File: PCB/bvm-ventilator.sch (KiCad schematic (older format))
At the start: 6 parts, among them U1 IEC_CONNECTOR

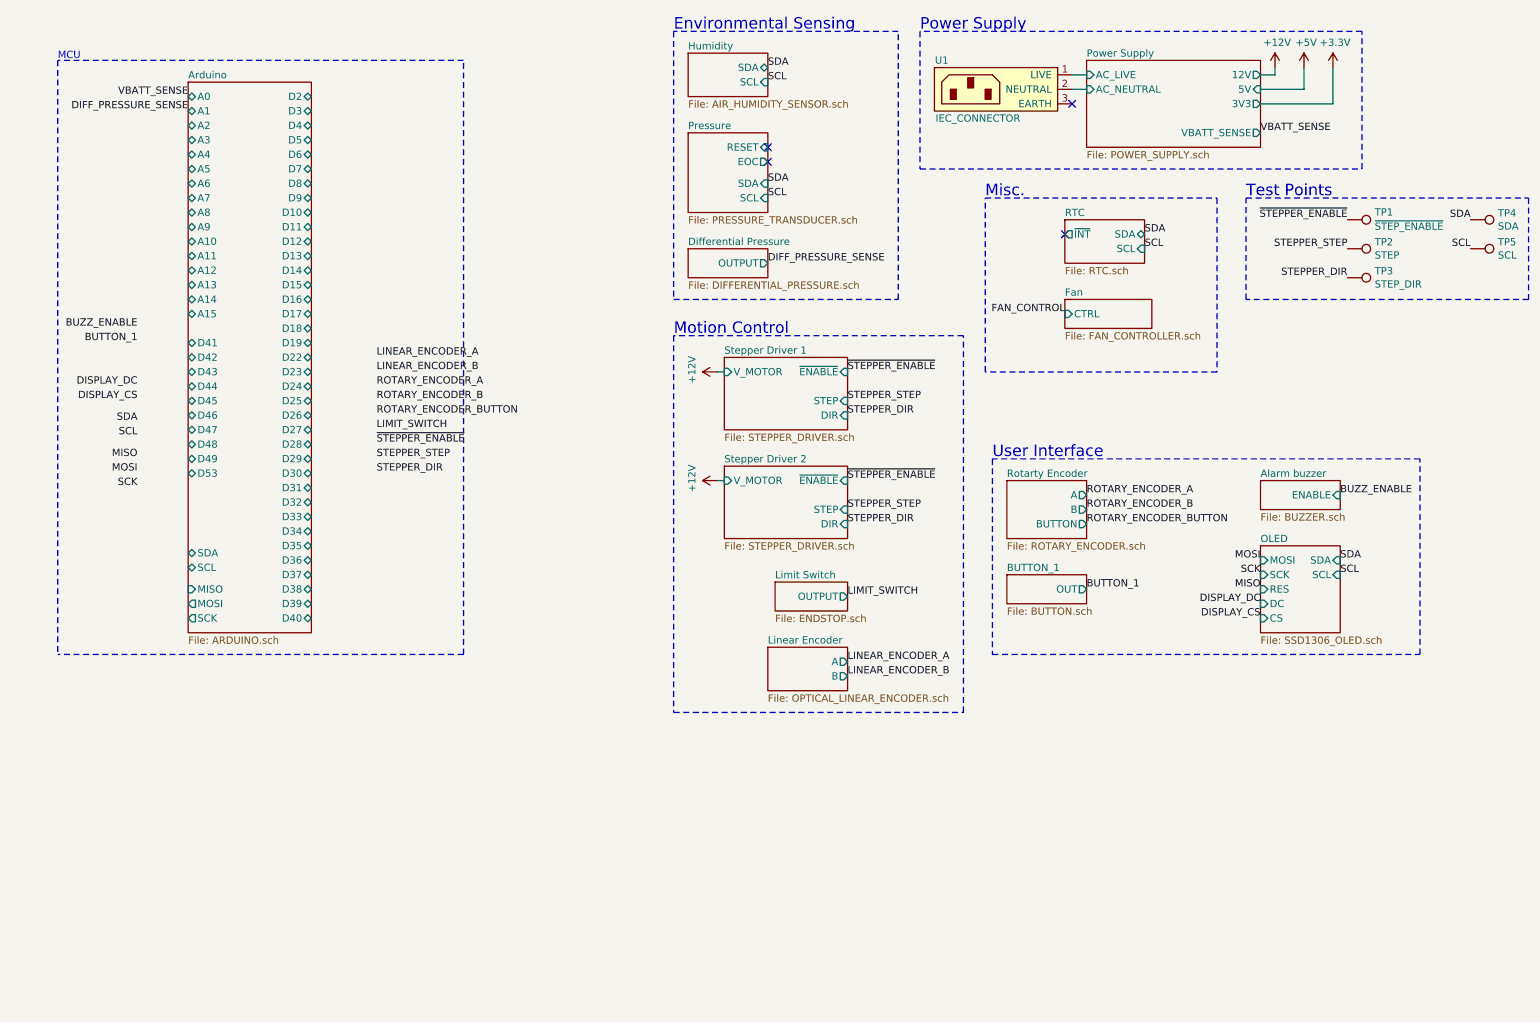
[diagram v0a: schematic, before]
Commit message: Connected all unconnected control/indicator pins
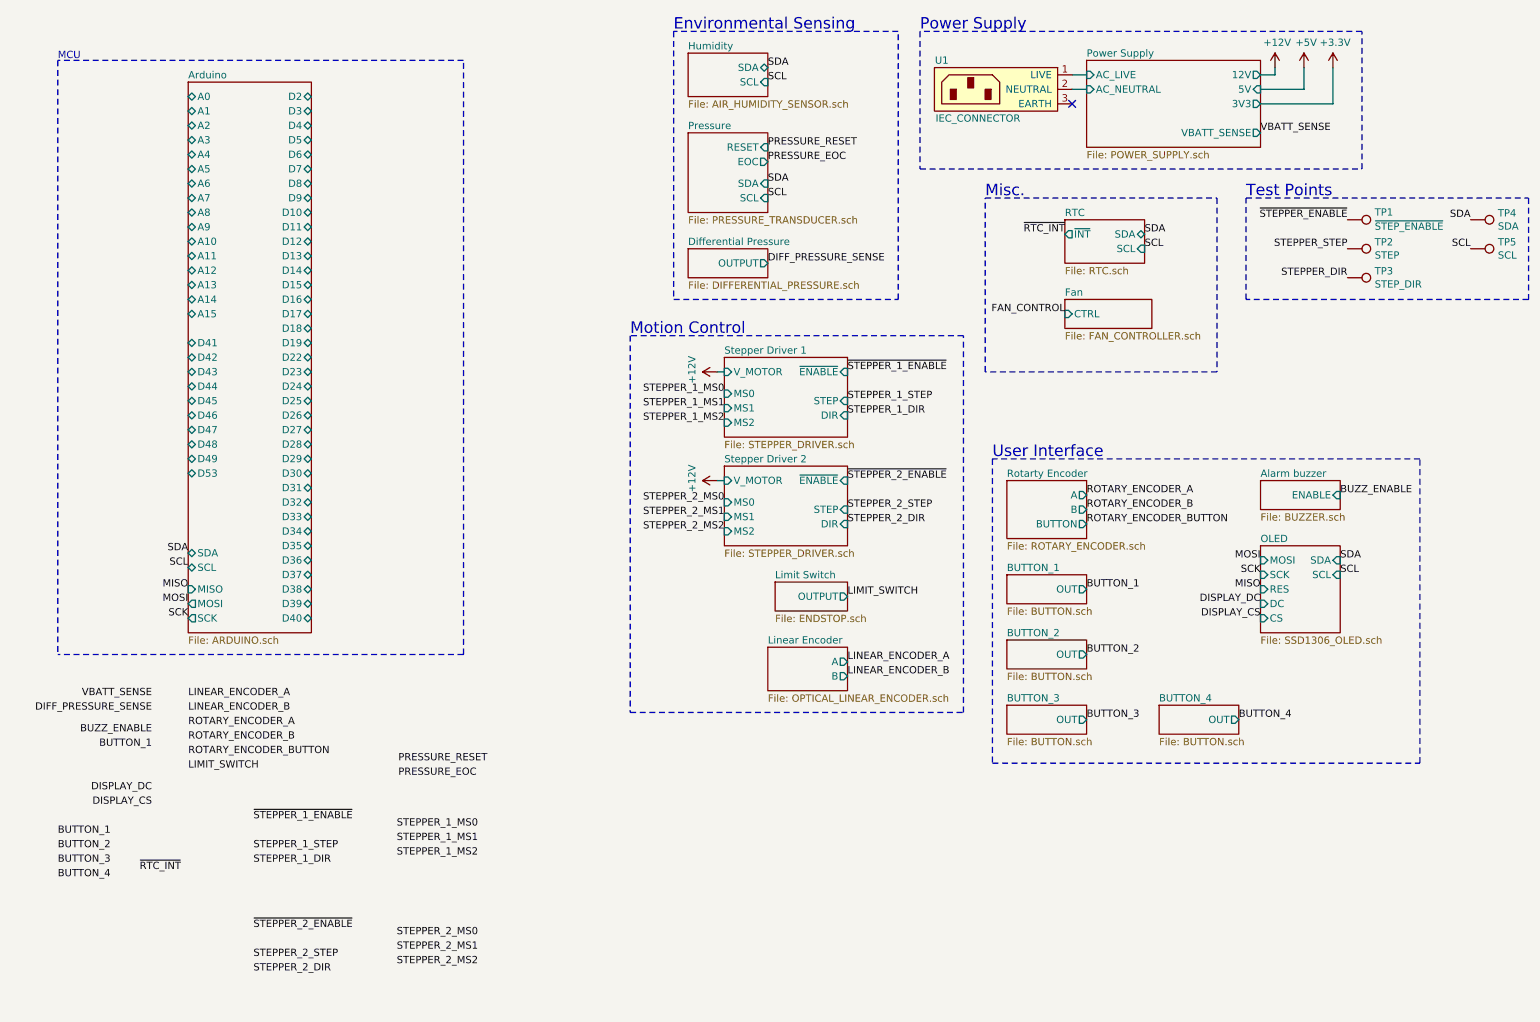
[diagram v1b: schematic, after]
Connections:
- no-connect marks 4 -> 1
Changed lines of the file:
@@
 $Descr A4 11693 8268
 encoding utf-8
-Sheet 1 23
+Sheet 1 26
 Title "ResQVenT"
 Date ""
@@
 $EndDescr
 $Sheet
-S 5450 3050 850  500
+S 5450 3050 850  550
 U 5E8A6686
 F0 "Stepper Driver 1" 50
@@
 F4 "DIR" I R 6300 3450 50
 F5 "~ENABLE" I R 6300 3150 50
+F6 "MS0" I L 5450 3300 50
+F7 "MS1" I L 5450 3400 50
+F8 "MS2" I L 5450 3500 50
 $EndSheet
 $Sheet
@@
 F5 "SDA" I R 5750 1850 50
 $EndSheet
-NoConn ~ 5750 1600
-NoConn ~ 5750 1700
 $Sheet
 S 7950 1000 1200 600
@@
 $EndSheet
 $Sheet
-S 5450 3800 850  500
+S 5450 3800 850  550
 U 5E8813FF
 F0 "Stepper Driver 2" 50
@@
 F4 "DIR" I R 6300 4200 50
 F5 "~ENABLE" I R 6300 3900 50
+F6 "MS0" I L 5450 4050 50
+F7 "MS1" I L 5450 4150 50
+F8 "MS2" I L 5450 4250 50
 $EndSheet
 $Sheet
@@
 F2 "OUTPUT" O R 6300 4700 50
 $EndSheet
-Text Label 1400 3500 2    50   ~ 0
+Text Label 1750 4400 2    50   ~ 0
 SDA
-Text Label 1400 3600 2    50   ~ 0
+Text Label 1750 4500 2    50   ~ 0
 SCL
 Text Label 9700 4450 0    50   ~ 0
@@
 SCL
 Text Label 6300 3350 0    50   ~ 0
-STEPPER_STEP
+STEPPER_1_STEP
 Text Label 6300 3450 0    50   ~ 0
-STEPPER_DIR
+STEPPER_1_DIR
 Text Label 6300 4100 0    50   ~ 0
-STEPPER_STEP
+STEPPER_2_STEP
 Text Label 6300 4200 0    50   ~ 0
-STEPPER_DIR
-Text Label 3050 3750 0    50   ~ 0
-STEPPER_STEP
-Text Label 3050 3850 0    50   ~ 0
-STEPPER_DIR
+STEPPER_2_DIR
 Text Label 9700 4000 0    50   ~ 0
 BUZZ_ENABLE
-Text Label 1400 2850 2    50   ~ 0
+Text Label 1500 5650 2    50   ~ 0
 BUZZ_ENABLE
-NoConn ~ 7800 2200
-Text Label 3050 3550 0    50   ~ 0
+Text Label 1750 5900 0    50   ~ 0
 LIMIT_SWITCH
 Text Label 6300 4700 0    50   ~ 0
 LIMIT_SWITCH
 Text Label 6300 3900 0    50   ~ 0
-~STEPPER_ENABLE
-Text Label 1750 1250 2    50   ~ 0
+~STEPPER_2_ENABLE
+Text Label 1500 5400 2    50   ~ 0
 VBATT_SENSE
 $Sheet
@@
 Text Label 7950 4200 0    50   ~ 0
 ROTARY_ENCODER_BUTTON
-Text Label 3050 3250 0    50   ~ 0
+Text Label 1750 5600 0    50   ~ 0
 ROTARY_ENCODER_A
-Text Label 3050 3350 0    50   ~ 0
+Text Label 1750 5700 0    50   ~ 0
 ROTARY_ENCODER_B
-Text Label 3050 3450 0    50   ~ 0
+Text Label 1750 5800 0    50   ~ 0
 ROTARY_ENCODER_BUTTON
 $Sheet
@@
 Text Label 7950 4650 0    50   ~ 0
 BUTTON_1
-Text Label 1400 2950 2    50   ~ 0
+Text Label 1500 5750 2    50   ~ 0
 BUTTON_1
 Text Label 6300 3150 0    50   ~ 0
-~STEPPER_ENABLE
-Text Label 3050 3650 0    50   ~ 0
-~STEPPER_ENABLE
+~STEPPER_1_ENABLE
 $Comp
 L power:+12V #PWR03
@@
 Text Label 6300 5250 0    50   ~ 0
 LINEAR_ENCODER_B
-Text Label 3050 3050 0    50   ~ 0
+Text Label 1750 5400 0    50   ~ 0
 LINEAR_ENCODER_A
-Text Label 3050 3150 0    50   ~ 0
+Text Label 1750 5500 0    50   ~ 0
 LINEAR_ENCODER_B
 $Sheet
@@
 Text Label 5750 2400 0    50   ~ 0
 DIFF_PRESSURE_SENSE
-Text Label 1750 1350 2    50   ~ 0
+Text Label 1500 5500 2    50   ~ 0
 DIFF_PRESSURE_SENSE
 Text Label 5750 1050 0    50   ~ 0
@@
 	9450 1200 9450 1050
 Wire Notes Line
-	5100 2900 5100 5500
-Wire Notes Line
-	5100 5500 7100 5500
+	4800 2900 4800 5500
+Wire Notes Line
+	4800 5500 7100 5500
 Wire Notes Line
 	7100 5500 7100 2900
 Wire Notes Line
-	7100 2900 5100 2900
+	7100 2900 4800 2900
 Wire Notes Line
 	850  1000 850  5100
@@
 Wire Notes Line
 	6650 800  5100 800
-Text Label 1400 3750 2    50   ~ 0
+Text Label 1750 4650 2    50   ~ 0
 MISO
-Text Label 1400 3850 2    50   ~ 0
+Text Label 1750 4750 2    50   ~ 0
 MOSI
-Text Label 1400 3950 2    50   ~ 0
+Text Label 1750 4850 2    50   ~ 0
 SCK
-Text Label 1400 3350 2    50   ~ 0
-DISPLAY_CS
-Text Label 1400 3250 2    50   ~ 0
-DISPLAY_DC
 Text Label 9150 4750 2    50   ~ 0
 DISPLAY_DC
@@
 SCK
 Wire Notes Line
-	7300 3750 7300 5100
-Wire Notes Line
-	7300 5100 10250 5100
-Wire Notes Line
-	10250 5100 10250 3750
+	7300 3750 7300 5850
+Wire Notes Line
+	7300 5850 10250 5850
+Wire Notes Line
+	10250 5850 10250 3750
 Wire Notes Line
 	10250 3750 7300 3750
-Text Notes 5100 2900 0    79   ~ 0
+Text Notes 4800 2900 0    79   ~ 0
 Motion Control
 Text Notes 850  1000 0    50   ~ 0
@@
 Wire Notes Line
 	3650 5100 850  5100
+Text Label 7800 2200 2    50   ~ 0
+~RTC_INT
+Text Label 1700 6600 2    50   ~ 0
+~RTC_INT
+Text Label 2200 6450 0    50   ~ 0
+STEPPER_1_STEP
+Text Label 2200 6550 0    50   ~ 0
+STEPPER_1_DIR
+Text Label 2200 7200 0    50   ~ 0
+STEPPER_2_STEP
+Text Label 2200 7300 0    50   ~ 0
+STEPPER_2_DIR
+Text Label 2200 7000 0    50   ~ 0
+~STEPPER_2_ENABLE
+Text Label 2200 6250 0    50   ~ 0
+~STEPPER_1_ENABLE
+Text Label 5450 3300 2    50   ~ 0
+STEPPER_1_MS0
+Text Label 5450 3400 2    50   ~ 0
+STEPPER_1_MS1
+Text Label 5450 3500 2    50   ~ 0
+STEPPER_1_MS2
+Text Label 5450 4050 2    50   ~ 0
+STEPPER_2_MS0
+Text Label 5450 4150 2    50   ~ 0
+STEPPER_2_MS1
+Text Label 5450 4250 2    50   ~ 0
+STEPPER_2_MS2
+Text Label 3750 6300 2    50   ~ 0
+STEPPER_1_MS0
+Text Label 3750 6400 2    50   ~ 0
+STEPPER_1_MS1
+Text Label 3750 6500 2    50   ~ 0
+STEPPER_1_MS2
+Text Label 3750 7050 2    50   ~ 0
+STEPPER_2_MS0
+Text Label 3750 7150 2    50   ~ 0
+STEPPER_2_MS1
+Text Label 3750 7250 2    50   ~ 0
+STEPPER_2_MS2
+Text Label 5750 1600 0    50   ~ 0
+PRESSURE_RESET
+Text Label 5750 1700 0    50   ~ 0
+PRESSURE_EOC
+Text Label 3200 5850 0    50   ~ 0
+PRESSURE_RESET
+Text Label 3200 5950 0    50   ~ 0
+PRESSURE_EOC
+$Sheet
+S 7400 5000 550  200
+U 5E96853E
+F0 "BUTTON_2" 50
+F1 "BUTTON.sch" 50
+F2 "OUT" O R 7950 5100 50
+$EndSheet
+Text Label 7950 5100 0    50   ~ 0
+BUTTON_2
+$Sheet
+S 7400 5450 550  200
+U 5E968934
+F0 "BUTTON_3" 50
+F1 "BUTTON.sch" 50
+F2 "OUT" O R 7950 5550 50
+$EndSheet
+Text Label 7950 5550 0    50   ~ 0
+BUTTON_3
+$Sheet
+S 8450 5450 550  200
+U 5E968D0C
+F0 "BUTTON_4" 50
+F1 "BUTTON.sch" 50
+F2 "OUT" O R 9000 5550 50
+$EndSheet
+Text Label 9000 5550 0    50   ~ 0
+BUTTON_4
+Text Label 850  6450 0    50   ~ 0
+BUTTON_2
+Text Label 850  6550 0    50   ~ 0
+BUTTON_3
+Text Label 850  6650 0    50   ~ 0
+BUTTON_4
+Text Label 850  6350 0    50   ~ 0
+BUTTON_1
+Text Label 1500 6050 2    50   ~ 0
+DISPLAY_DC
+Text Label 1500 6150 2    50   ~ 0
+DISPLAY_CS
 $EndSCHEMATC
